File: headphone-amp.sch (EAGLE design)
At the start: 46 parts, among them IC1 OPA1612, J1 USB4125-GF-A_REVA, J3 PJ-3200, J4 PJ-3200, J5 PJ-3200, U1 TPS65131

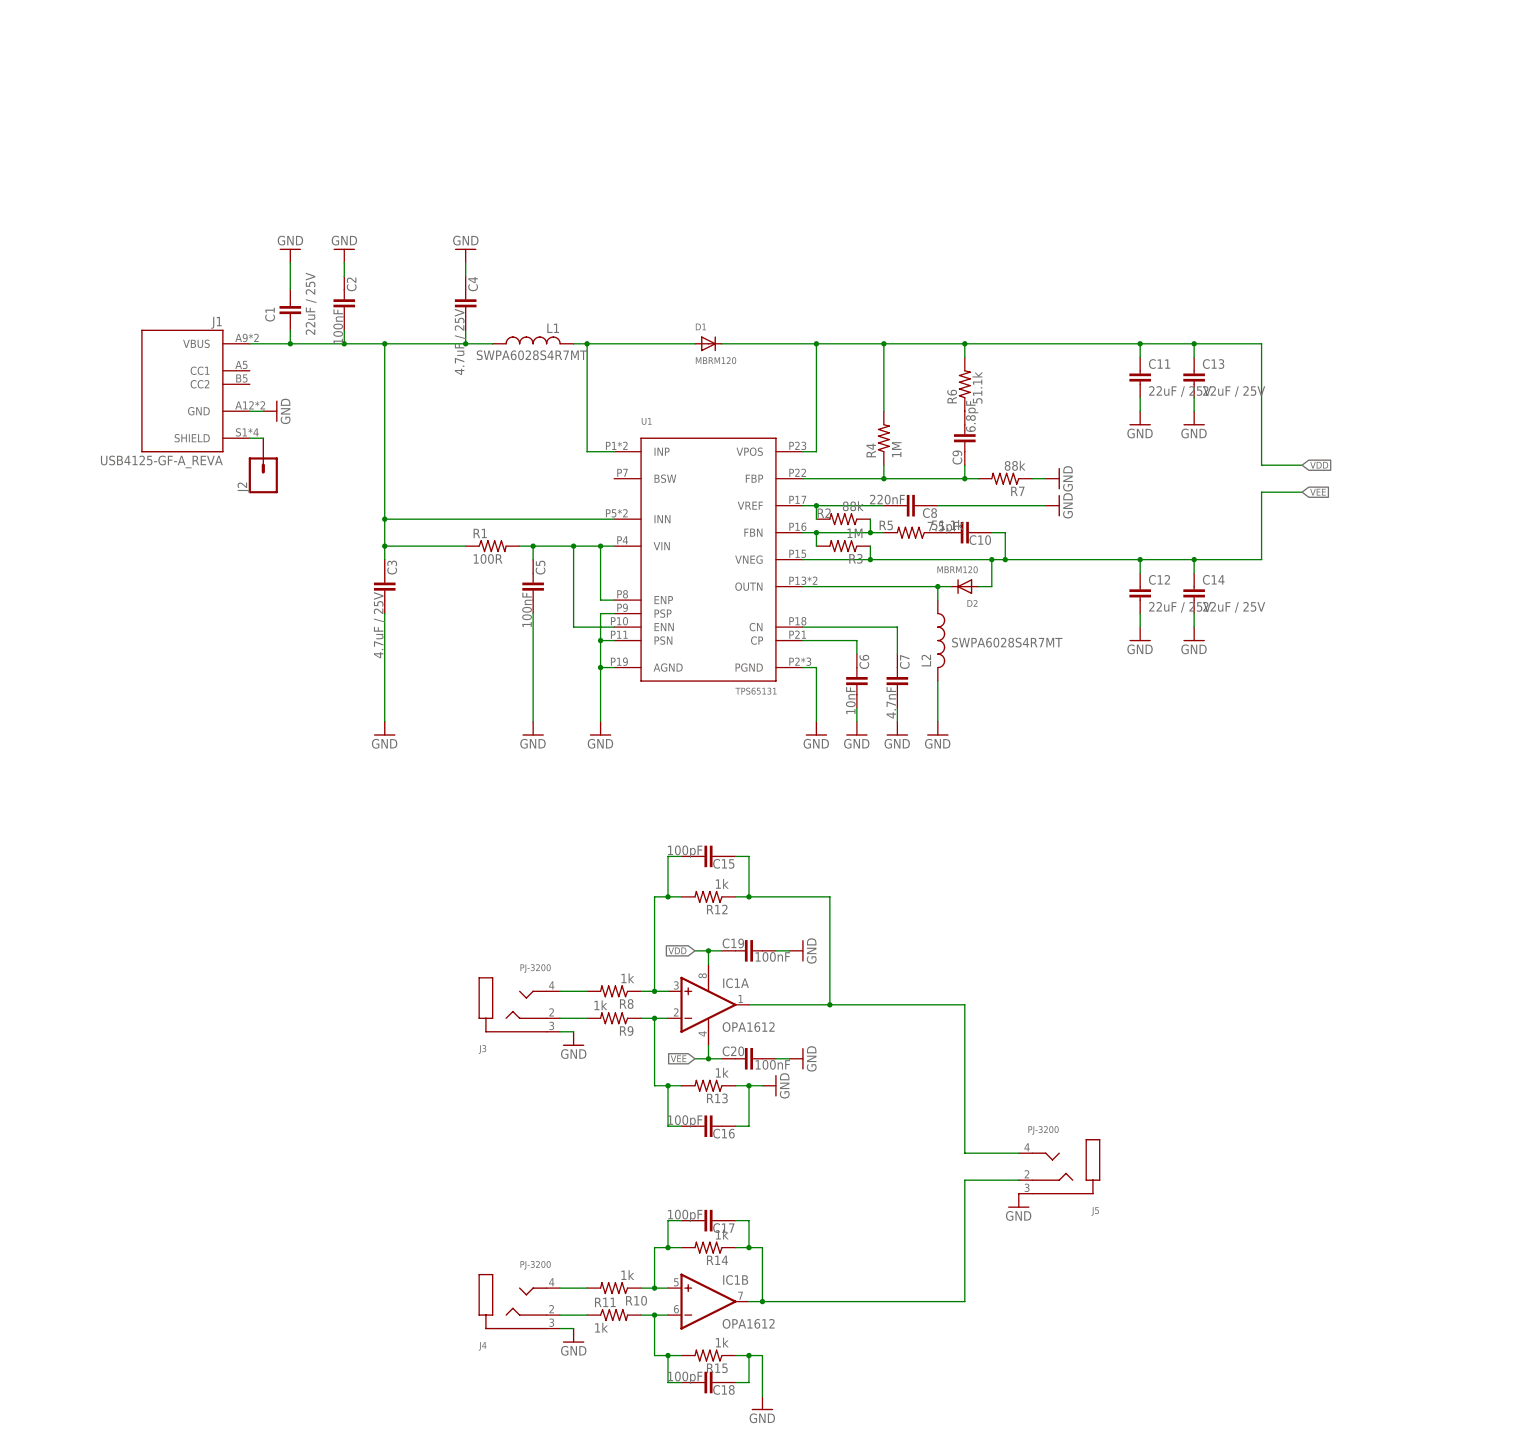
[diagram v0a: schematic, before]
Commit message: add power led, add soft start, fix op amp polarity
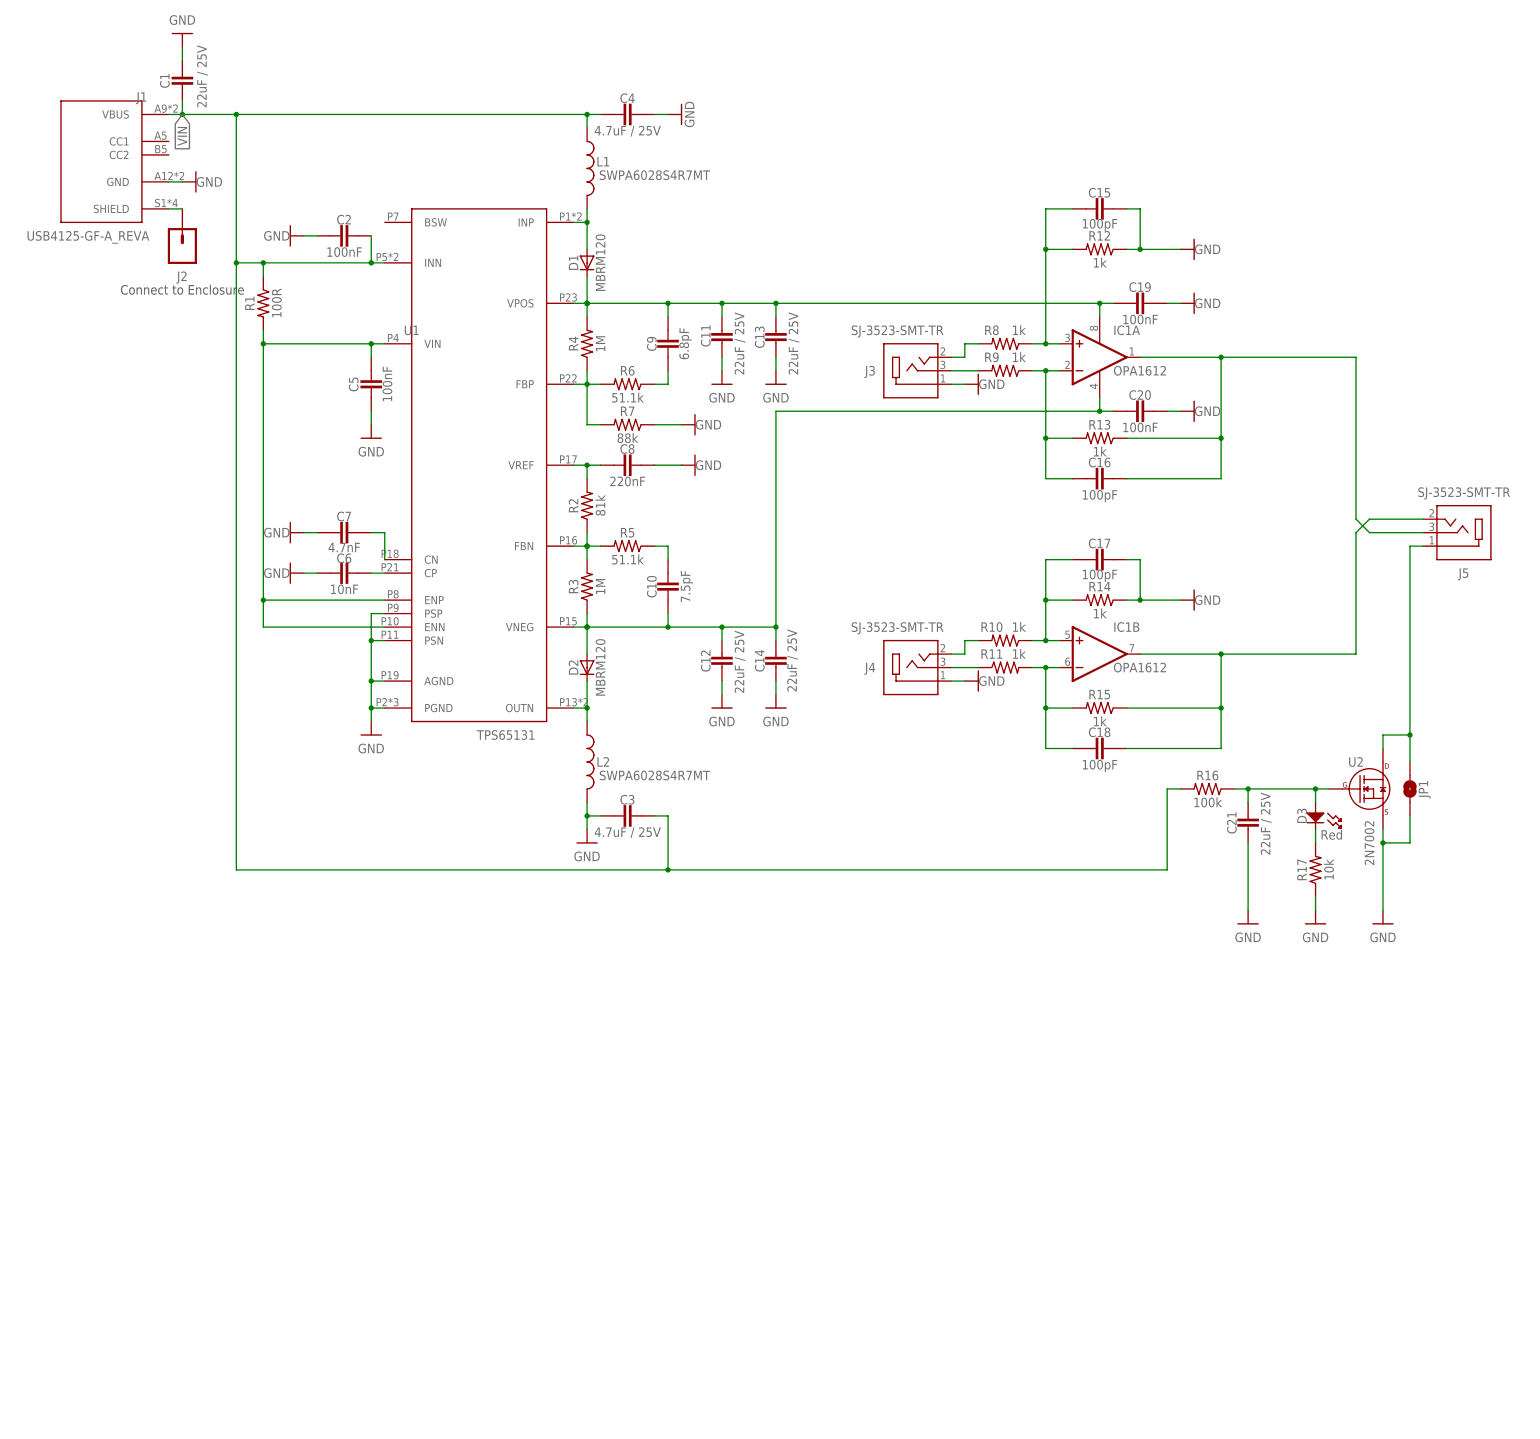
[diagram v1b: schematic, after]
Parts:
- added C21: 22uF / 25V, rcl:C-EUC0805
- added D3: Red, MF_LEDs:LED_SINGLE-0603
- added JP1: JUMPER-SMT_2_NO_SILK, SparkFun-Jumpers:JUMPER-SMT_2_NO_SILK
- added R16: 100k, rcl:R-US_R0402
- added R17: 10k, rcl:R-US_R0402
- added U2: 2N7002, MF_Discrete_Semiconductor:N-CHANNEL_FET_SOT-23-3
- J3, J4, J5: value PJ-3200 -> SJ-3523-SMT-TR; device sonik:3.5MMSTEREOJACK -> SJ-3523-SMT-TR:SJ-3523-SMT-TR
- R2: value 88k -> 81k
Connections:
- removed net N$2: C1.2, C2.2, C3.1, C4.2, J1.VBUS, L1.1, R1.1, U1.INN
- removed net N$23 (its old number): C15.1, IC1A.OUT, J5.T, R12.1
- new net N$1: C18.1, IC1B.OUT, J5.2, R15.1
- new net N$25: J5.1, JP1.2, U2.DRAIN
- new net N$26: C21.1, D3.ANODE, R16.1, U2.GATE
- new net N$4: C16.1, IC1A.OUT, J5.3, R13.1
- new net VIN: C1.2, C2.2, C3.1, C4.2, J1.VBUS, L1.1, R1.1, R16.2, U1.INN
- net GND: now also C15.1, C17.1, C21.2, J3.1, J4.1, JP1.1, R12.1, R14.1, R17.1, U2.SOURCE; no longer C16.1, C18.1, J3.S, J4.S, J5.S, R13.1, R15.1
- net N$12: now also J3.2, R8.2; no longer J3.R, R9.2
- net N$18: now also J4.2; no longer J4.T
- net N$19: now also J4.3; no longer J4.R
- net N$20: now also D3.CATHODE, R17.2; no longer C17.1, IC1B.OUT, J5.R, R14.1
- net N$6: now also J3.3, R9.2; no longer J3.T, R8.2
- net N$7: now also R6.2; no longer C9.1
- net VDD: now also C9.1; no longer R6.2
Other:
- note added: "Connect to Enclosure"
- moved on the sheet: C1, C10, C11, C12, C13, C14, C15, C16, C17, C18, C19, C2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
